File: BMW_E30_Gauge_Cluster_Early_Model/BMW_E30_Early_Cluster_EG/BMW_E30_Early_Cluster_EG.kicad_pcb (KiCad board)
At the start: 2 copper layers, 20.8 x 12.8 mm, 0 parts

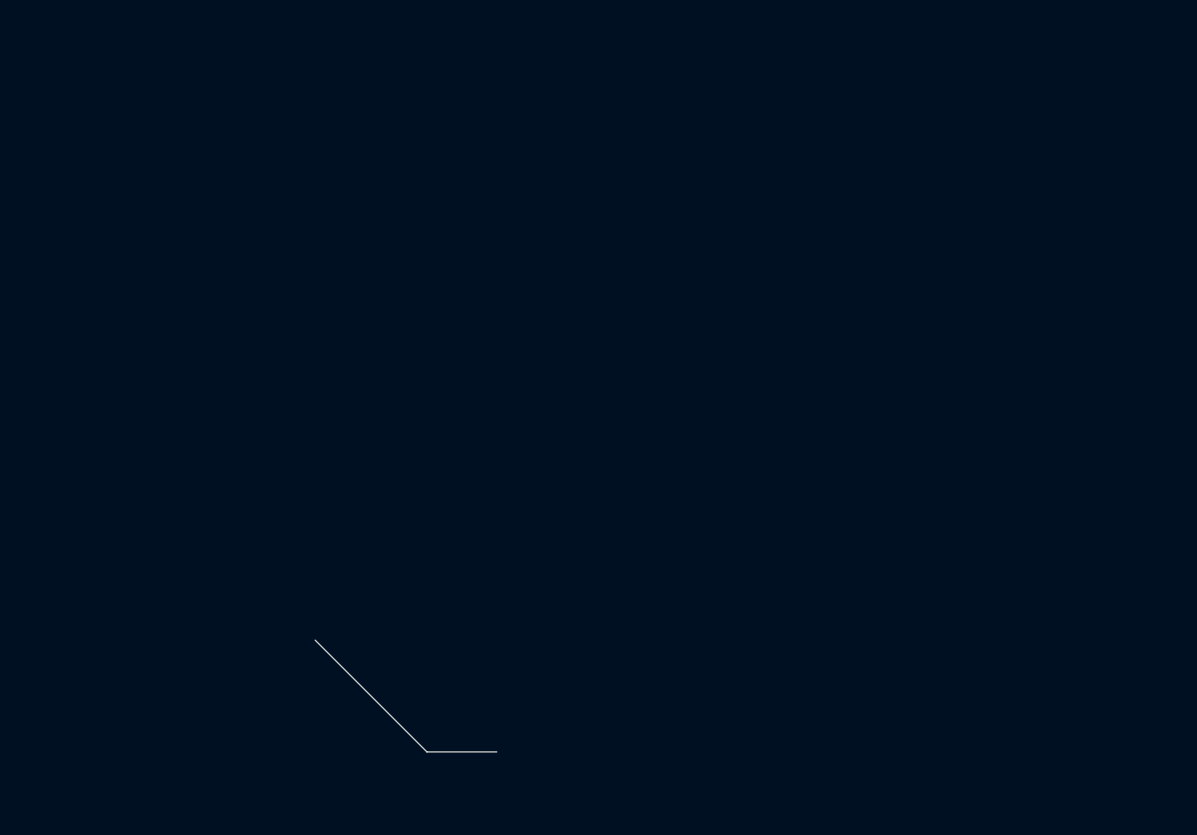
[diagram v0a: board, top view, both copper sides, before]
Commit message: Layout Updates for EG
TODO: fix reference designators that were rewritten by accident. Original reference designators are listed in the schematic pdf.
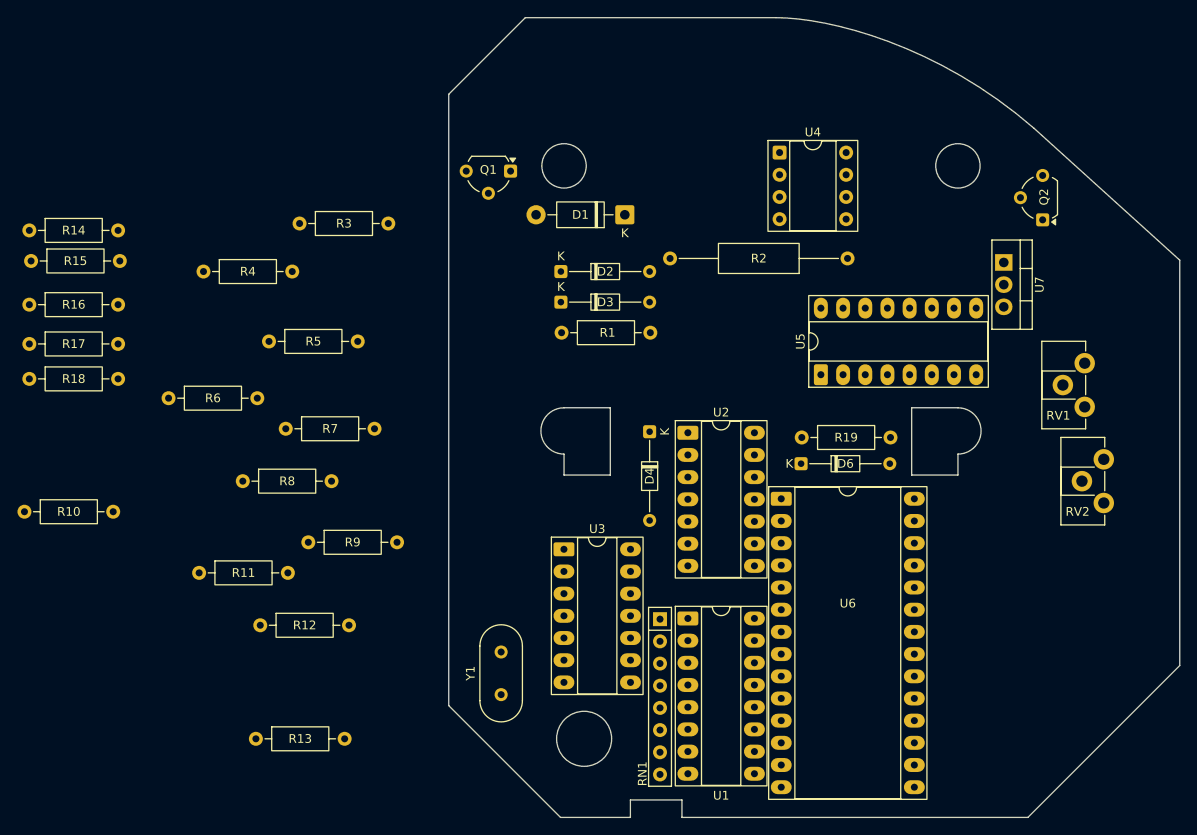
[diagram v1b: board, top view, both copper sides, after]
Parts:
- added D1: 1N4004, Diode_THT:D_DO-41_SOD81_P10.16mm_Horizontal, F.Cu at (139.7, 63.5)
- added D2: 1N1418, Diode_THT:D_DO-34_SOD68_P10.16mm_Horizontal, F.Cu at (132.3, 70.0)
- added D3: 1N1418, Diode_THT:D_DO-34_SOD68_P10.16mm_Horizontal, F.Cu at (132.3, 73.5)
- added D4: 1N1418, Diode_THT:D_DO-34_SOD68_P10.16mm_Horizontal, F.Cu at (142.5, 88.3)
- added D6: 1N1418, Diode_THT:D_DO-34_SOD68_P10.16mm_Horizontal, F.Cu at (159.8, 92.0)
- added Q1: BC547C, Package_TO_SOT_THT:TO-92L_Wide, F.Cu at (126.6, 58.5)
- added Q2: BC337, Package_TO_SOT_THT:TO-92L_Wide, F.Cu at (187.5, 64.1)
- added R1: 10k, Resistor_THT:R_Axial_DIN0207_L6.3mm_D2.5mm_P10.16mm_Horizontal, F.Cu at (132.4, 77.0)
- added R10: 100k, Resistor_THT:R_Axial_DIN0207_L6.3mm_D2.5mm_P10.16mm_Horizontal, F.Cu at (70.9, 97.5)
- added R11: 47k, Resistor_THT:R_Axial_DIN0207_L6.3mm_D2.5mm_P10.16mm_Horizontal, F.Cu at (90.9, 104.5)
- added R12: 10k, Resistor_THT:R_Axial_DIN0207_L6.3mm_D2.5mm_P10.16mm_Horizontal, F.Cu at (97.9, 110.5)
- added R13: 10k, Resistor_THT:R_Axial_DIN0207_L6.3mm_D2.5mm_P10.16mm_Horizontal, F.Cu at (97.4, 123.5)
- added R14: 2k7, Resistor_THT:R_Axial_DIN0207_L6.3mm_D2.5mm_P10.16mm_Horizontal, F.Cu at (71.5, 65.3)
- added R15: 100k, Resistor_THT:R_Axial_DIN0207_L6.3mm_D2.5mm_P10.16mm_Horizontal, F.Cu at (71.7, 68.8)
- added R16: 100k, Resistor_THT:R_Axial_DIN0207_L6.3mm_D2.5mm_P10.16mm_Horizontal, F.Cu at (71.5, 73.8)
- added R17: 470k, Resistor_THT:R_Axial_DIN0207_L6.3mm_D2.5mm_P10.16mm_Horizontal, F.Cu at (71.5, 78.3)
- added R18: 47k, Resistor_THT:R_Axial_DIN0207_L6.3mm_D2.5mm_P10.16mm_Horizontal, F.Cu at (71.5, 82.3)
- added R19: 120R, Resistor_THT:R_Axial_DIN0207_L6.3mm_D2.5mm_P10.16mm_Horizontal, F.Cu at (159.9, 89.0)
- added R2: 20R, Resistor_THT:R_Axial_DIN0309_L9.0mm_D3.2mm_P20.32mm_Horizontal, F.Cu at (165.2, 68.5)
- added R3: 16k, Resistor_THT:R_Axial_DIN0207_L6.3mm_D2.5mm_P10.16mm_Horizontal, F.Cu at (102.4, 64.5)
- added R4: 10k, Resistor_THT:R_Axial_DIN0207_L6.3mm_D2.5mm_P10.16mm_Horizontal, F.Cu at (91.4, 70.0)
- added R5: 47k, Resistor_THT:R_Axial_DIN0207_L6.3mm_D2.5mm_P10.16mm_Horizontal, F.Cu at (98.9, 78.0)
- added R6: 36k, Resistor_THT:R_Axial_DIN0207_L6.3mm_D2.5mm_P10.16mm_Horizontal, F.Cu at (87.4, 84.5)
- added R7: 39k, Resistor_THT:R_Axial_DIN0207_L6.3mm_D2.5mm_P10.16mm_Horizontal, F.Cu at (100.8, 88.0)
- added R8: 33k, Resistor_THT:R_Axial_DIN0207_L6.3mm_D2.5mm_P10.16mm_Horizontal, F.Cu at (95.9, 94.0)
- added R9: 803R 1%, Resistor_THT:R_Axial_DIN0207_L6.3mm_D2.5mm_P10.16mm_Horizontal, F.Cu at (103.4, 101.0)
- added RN1: R2R_8B, Resistor_THT:R_Array_SIP8, F.Cu at (143.7, 109.8)
- added RV1: 220k, Potentiometer_THT:Potentiometer_ACP_CA9-H2,5_Horizontal, F.Cu at (192.3, 85.5)
- added RV2: 220k, Potentiometer_THT:Potentiometer_ACP_CA9-H2,5_Horizontal, F.Cu at (194.5, 96.5)
- added U1: 4049, Package_DIP:DIP-16_W7.62mm_Socket_LongPads, F.Cu at (146.9, 109.7)
- added U2: 4584, Package_DIP:DIP-14_W7.62mm_Socket_LongPads, F.Cu at (146.9, 88.5)
- added U3: SAJ300R, Package_DIP:DIP-14_W7.62mm_Socket_LongPads, F.Cu at (132.7, 101.8)
- added U4: LM2903, Package_DIP:DIP-8_W7.62mm_Socket, F.Cu at (157.4, 56.4)
- added U5: SCL4527B, Package_DIP:DIP-16_W7.62mm_Socket_LongPads, F.Cu at (162.1, 81.8)
- added U6: PIC1655A, Package_DIP:DIP-28_W15.24mm_Socket_LongPads, F.Cu at (157.6, 96.0)
- added U7: LM2930-5.0_TO220, Package_TO_SOT_THT:TO-220-3_Vertical, F.Cu at (183.1, 69.0)
- added Y1: 160 kHz, Crystal:Crystal_HC49-U_Vertical, F.Cu at (125.5, 113.6)
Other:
- board size 20.8 x 12.8 mm -> 83.7 x 91.6 mm

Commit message: EG Layout Updates
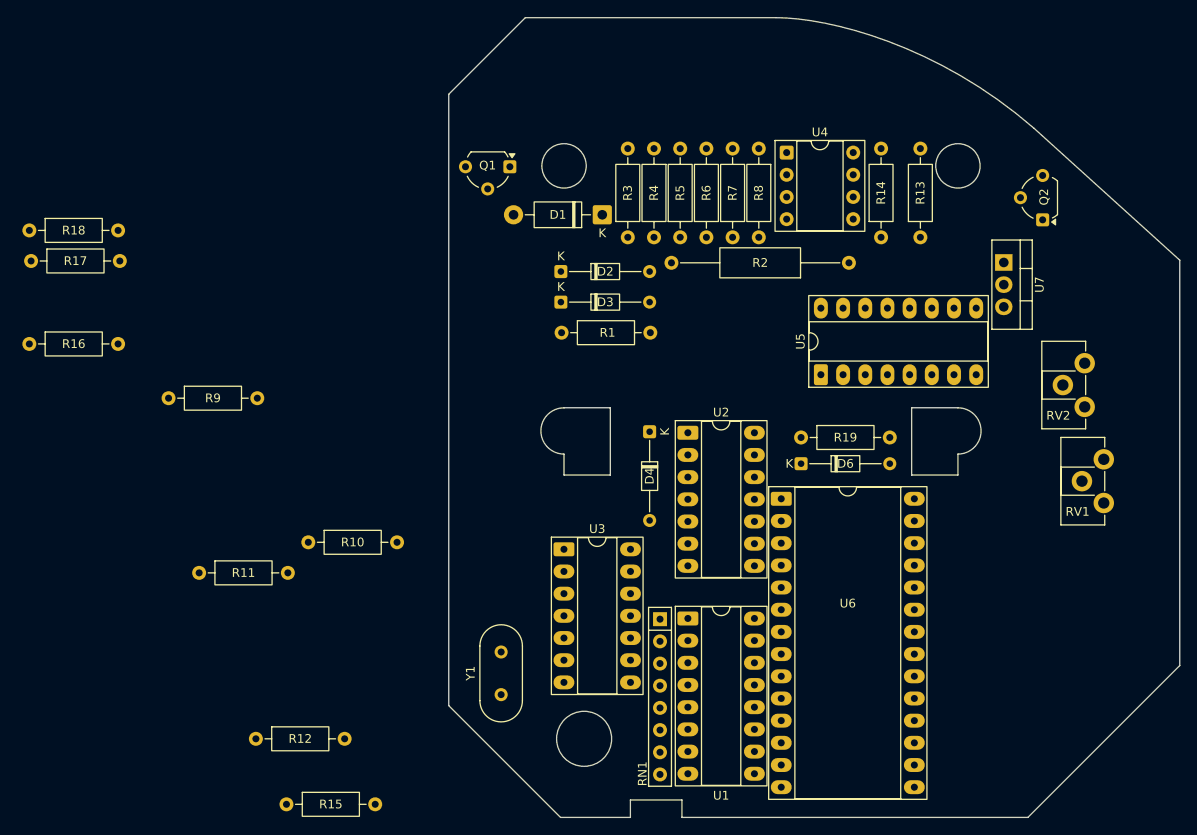
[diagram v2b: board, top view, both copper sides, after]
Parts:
- moved R14 98.9 mm to (169.0, 66.1), turned to 90 degrees
- moved R8 93.8 mm to (155.0, 55.9), turned to -90 degrees
- moved R19 89.7 mm to (159.8, 89.0)
- moved R13 87.7 mm to (173.5, 66.1), turned to 90 degrees
- moved R15 72.4 mm to (100.9, 131.0)
- moved R7 62.6 mm to (152.0, 66.1), turned to 90 degrees
- moved R6 52.9 mm to (149.0, 66.1), turned to 90 degrees
- moved R4 49.3 mm to (143.0, 55.9), turned to -90 degrees
- moved R3 48.7 mm to (140.0, 66.1), turned to 90 degrees
- moved R5 43.6 mm to (146.0, 66.1), turned to 90 degrees
- moved D1 2.58 mm to (137.1, 63.5)
- moved U4 0.81 mm to (158.2, 56.4)
- moved R2 0.52 mm to (165.3, 69.0)
- moved Q1 0.51 mm to (126.5, 58.0)
- renumbered R9 to R10, R13 to R12, R12 to R13, R18 to R14, R19 to R15, R17 to R16, R15 to R17, R14 to R18, R16 to R19, R4 to R3, R5 to R4, R3 to R5, R7 to R6, R8 to R7, R10 to R8, R6 to R9, RV2 to RV1, RV1 to RV2

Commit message: EG Layout Updates
Added capacitor footprints and moved all resistors into place.
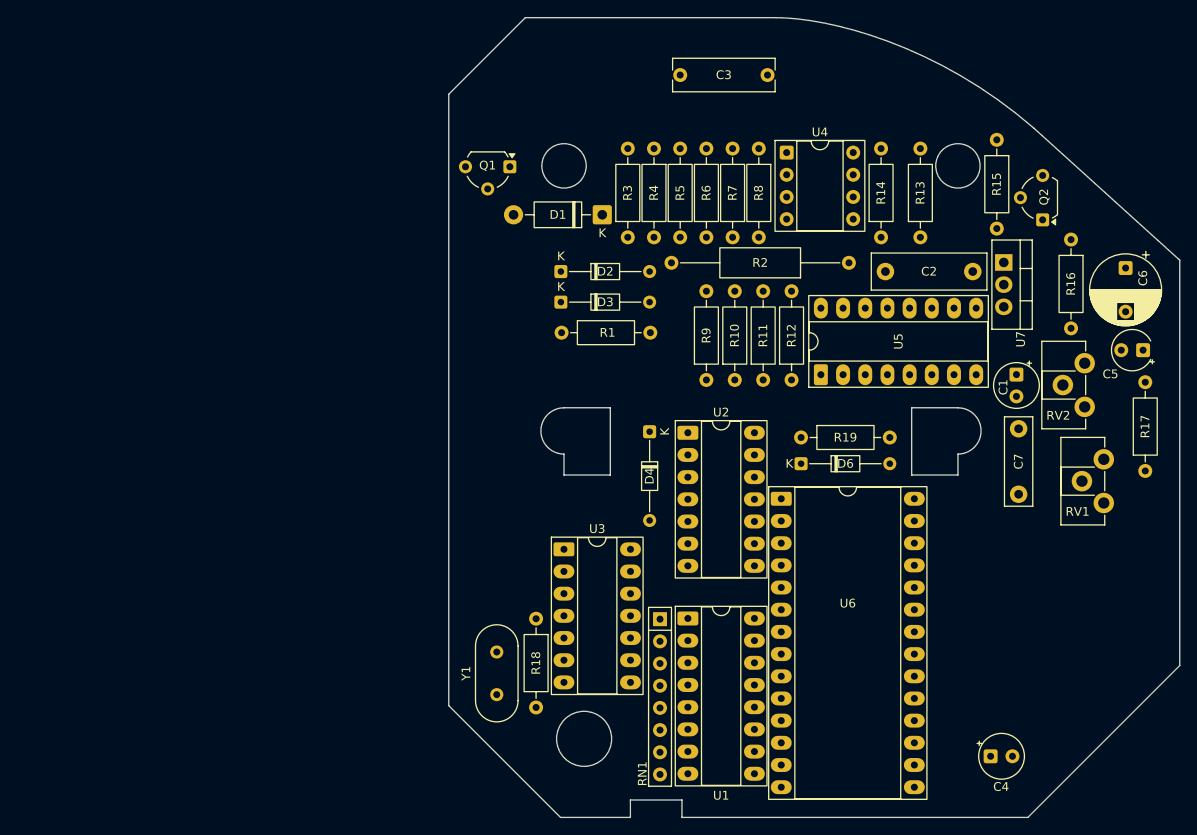
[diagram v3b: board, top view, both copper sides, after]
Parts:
- added C1: 47u, Capacitor_THT:CP_Radial_Tantal_D5.0mm_P2.50mm, F.Cu at (184.5, 81.8)
- added C2: 33n, Capacitor_THT:C_Rect_L13.0mm_W4.0mm_P10.00mm_FKS3_FKP3_MKS4, F.Cu at (169.5, 70.0)
- added C3: 47n, Capacitor_THT:C_Rect_L11.5mm_W3.6mm_P10.00mm_MKT, F.Cu at (156.0, 47.5)
- added C4: 1u, Capacitor_THT:CP_Radial_Tantal_D5.0mm_P2.50mm, F.Cu at (181.5, 125.5)
- added C5: 2.2u, Capacitor_THT:CP_Radial_Tantal_D4.5mm_P2.50mm, F.Cu at (199.0, 79.0)
- added C6: 100u, Capacitor_THT:CP_Radial_D8.0mm_P5.00mm, F.Cu at (197.0, 69.6)
- added C7: 0.22u, Capacitor_THT:C_Rect_L10.0mm_W3.0mm_P7.50mm_FKS3_FKP3, F.Cu at (184.8, 95.5)
- moved R17 129.8 mm to (199.2, 92.8), turned to 90 degrees
- moved R16 119.9 mm to (190.8, 66.3), turned to -90 degrees
- moved R15 111.4 mm to (182.2, 54.9), turned to -90 degrees
- moved R12 73.8 mm to (158.8, 82.4), turned to 90 degrees
- moved R18 73.1 mm to (129.5, 109.8), turned to -90 degrees
- moved R11 68.3 mm to (155.5, 82.4), turned to 90 degrees
- moved R9 61.6 mm to (149.0, 82.4), turned to 90 degrees
- moved R10 52.2 mm to (152.2, 82.4), turned to 90 degrees
- moved Y1 0.50 mm to (125.0, 113.6)

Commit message: Layout Updates
Added footprints for coding plug, econometer gauge, and D5.

Also fixed pin number 28 on U6.
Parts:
- added D5: BZX55C 18V, Diode_THT:D_DO-34_SOD68_P10.16mm_Horizontal, F.Cu at (187.8, 66.3)
- added MES1: Fuel Economy Gauge, BMW_Cluster_Connectors:Connector_EG, F.Cu at (179.0, 124.1)
- added SW1: Coding Plug, BMW_Cluster_Connectors:Coding_Plug, F.Cu at (187.5, 110.4)
- U6: footprint Package_DIP:DIP-28_W15.24mm_Socket_LongPads -> Package_DIP:DIP-28_W15.24mm
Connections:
- U6 pad 26: Net-(D6-A) -> unconnected-(U6-CLKOUT-Pad26)
- U6 pad 28: (no net) -> Net-(D6-A)

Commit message: Layout Updates for EG
Added footprints for J1 and J2 connectors. Also Changed footprint for RN1 to match original board. Next step is to route traces.
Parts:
- added J1: Conn_01x11_Socket, BMW_Cluster_Connectors:ConnectorIV_EG_Socket, F.Cu at (125.5, 85.5)
- added J2: To EG, BMW_Cluster_Connectors:EG_Tach_Socket, F.Cu at (135.0, 47.5)
- C3: footprint Capacitor_THT:C_Rect_L11.5mm_W3.6mm_P10.00mm_MKT -> Capacitor_THT:C_Rect_L13.0mm_W4.0mm_P10.00mm_FKS3_FKP3_MKS4
- moved RN1 3.38 mm to (143.8, 106.4)
- moved C3 2.25 mm to (156.0, 45.2)

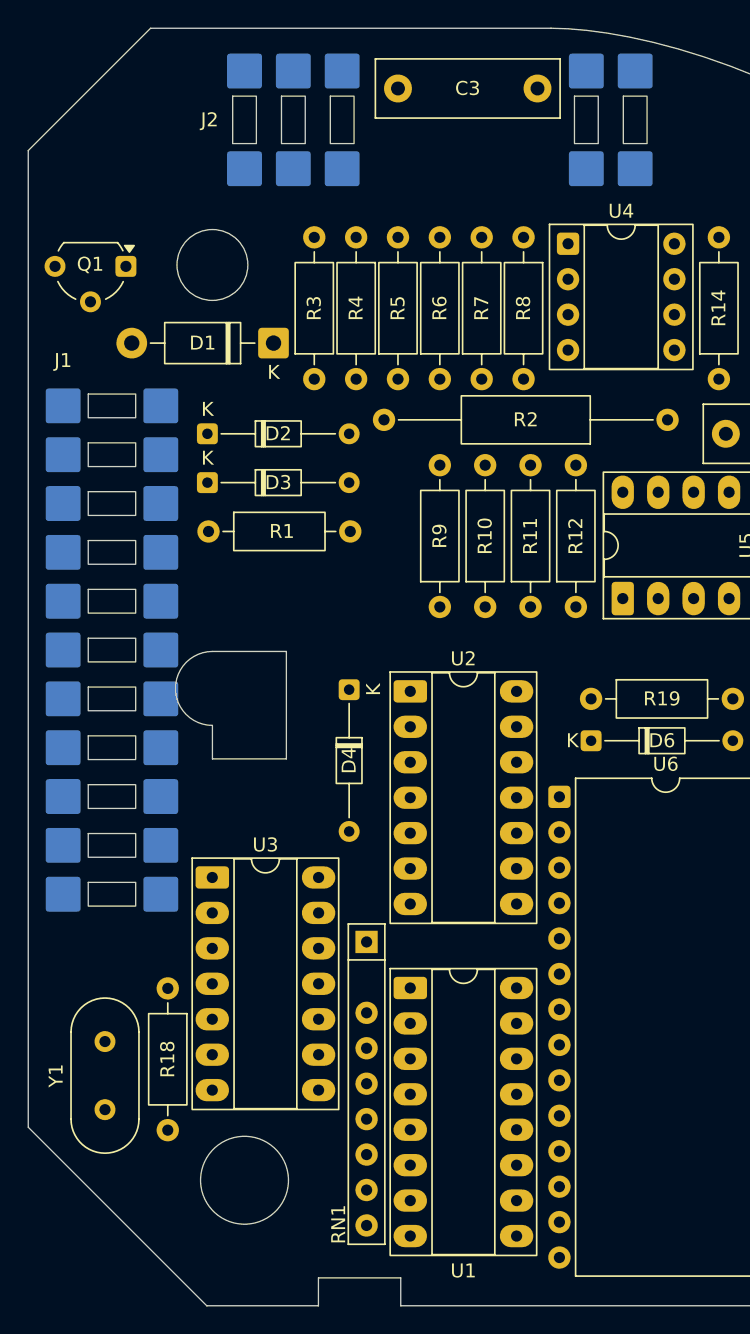
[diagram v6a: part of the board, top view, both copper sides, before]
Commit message: Layout for EG started
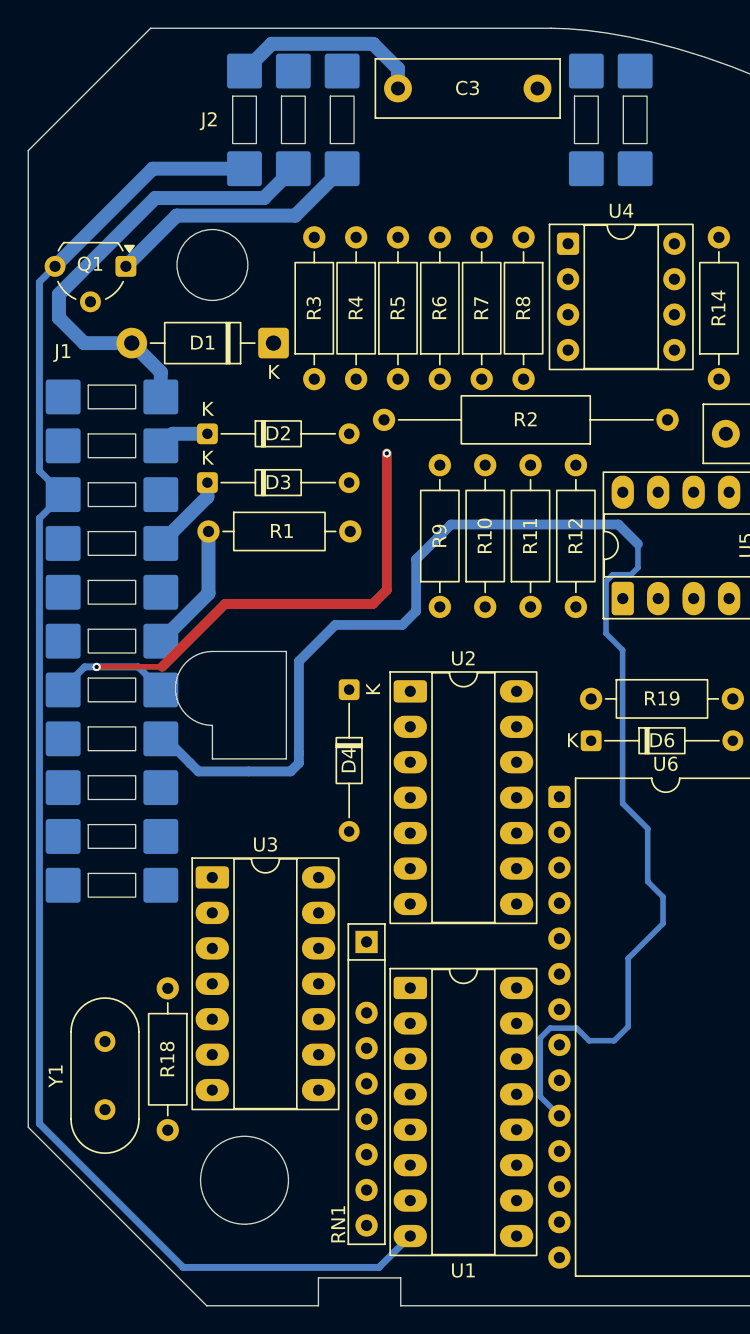
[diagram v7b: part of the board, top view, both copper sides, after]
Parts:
- moved J1 0.64 mm to (125.5, 84.9)
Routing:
- net GNDPWR: track 0.00 -> 125.5 mm
- net Dist_pulse: track 0.00 -> 102.1 mm
- net Speed_pulse: track 0.00 -> 41.3 mm, vias 0 -> 2
- net +12V T15: track 0.00 -> 32.9 mm
- net ~{6_cyl}: track 0.00 -> 18.4 mm
- net 6_cyl: track 0.00 -> 9.28 mm
- net Wheel_speed_output: track 0.00 -> 5.74 mm
- net Fuel_rate_input: track 0.00 -> 3.70 mm

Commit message: Layout Updates
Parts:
- U1: footprint Package_DIP:DIP-16_W7.62mm_Socket_LongPads -> Package_DIP:DIP-16_W7.62mm_Socket
- moved RV1 11.3 mm to (192.4, 85.4)
- moved RV2 11.2 mm to (194.5, 96.5)
- moved C2 10.3 mm to (179.8, 70.2), turned to 180 degrees
- moved R13 10.2 mm to (173.1, 55.9), turned to -90 degrees
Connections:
- R17 pad 1: Net-(RN1-Bit_out) -> Net-(RN1-R7)
- RN1 pad 1: Net-(RN1-Bit_out) -> GNDPWR
- RN1 pad 8: GNDPWR -> Net-(RN1-R7)
- RV2 pad 1: Net-(RN1-Bit_out) -> Net-(RN1-R7)
- RV2 pad 2: Net-(RN1-Bit_out) -> Net-(RN1-R7)
- U1 pad 10: Net-(RN1-R1) -> Net-(RN1-R6)
- U1 pad 12: Net-(RN1-R3) -> Net-(RN1-R4)
- U1 pad 15: Net-(RN1-R6) -> Net-(RN1-R1)
- U1 pad 2: Net-(RN1-R5) -> Net-(RN1-R2)
- U1 pad 4: Net-(RN1-R4) -> Net-(RN1-R3)
- U1 pad 6: Net-(RN1-R2) -> Net-(RN1-R5)
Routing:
- net GNDPWR: track 125.5 -> 385.7 mm
- net Net-(RN1-R7): track 0.00 -> 113.6 mm, vias 0 -> 2
- net +5V: track 0.00 -> 77.4 mm, vias 0 -> 2
- net VCC_T15: track 0.00 -> 58.5 mm
- net Net-(R12-Pad2): track 0.00 -> 40.4 mm
- net Net-(U3-CLK-Pad9): track 0.00 -> 32.2 mm
- net EG_B4: track 0.00 -> 29.3 mm
- net Net-(Q1-B): track 0.00 -> 28.0 mm
- net Net-(U3-CLK-Pad10): track 0.00 -> 26.5 mm
- net Net-(D4-A): track 0.00 -> 23.1 mm
- net EG_B5: track 0.00 -> 21.8 mm
- net EG_B1: track 0.00 -> 16.1 mm
- net Net-(RN1-R1): track 0.00 -> 15.8 mm
- net EG_B2: track 0.00 -> 15.0 mm
- net Net-(RN1-R6): track 0.00 -> 11.5 mm
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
